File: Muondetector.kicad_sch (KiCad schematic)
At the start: 32 parts, among them U2 ${SIM.PARAMS}, U3 ${SIM.PARAMS}

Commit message: yes
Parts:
- removed U7: ~, symbol MuonDetector:3965_pressure_sensor
- added C7: C, symbol Device:C
- added Q1, Q2: 2N7002E, Package_TO_SOT_SMD:SOT-23, symbol Transistor_FET:2N7002E
- added R14, R15, R16, R17, R18, R19, R20: R, symbol Device:R
- added U4: ~, symbol MuonDetector:MPR_Pressure_sensor
- added U7: ~, symbol MuonDetector:MIC5225
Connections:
- net at L1.2, R11.1, U2.3 (V+)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: now also R19.2, R20.2
- new net: Q1.2 (S), R15.1, R19.1
- new net: Q2.2 (S), R16.1, R20.1
- new net: Q1.3 (D), R17.1
- new net: Q1.1 (G), Q2.1 (G), R14.2, R17.2, R18.2
- new net: Q2.3 (D), R18.1
- new net +3.3V: R15.2, R16.2
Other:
- note added: "+3.3V"

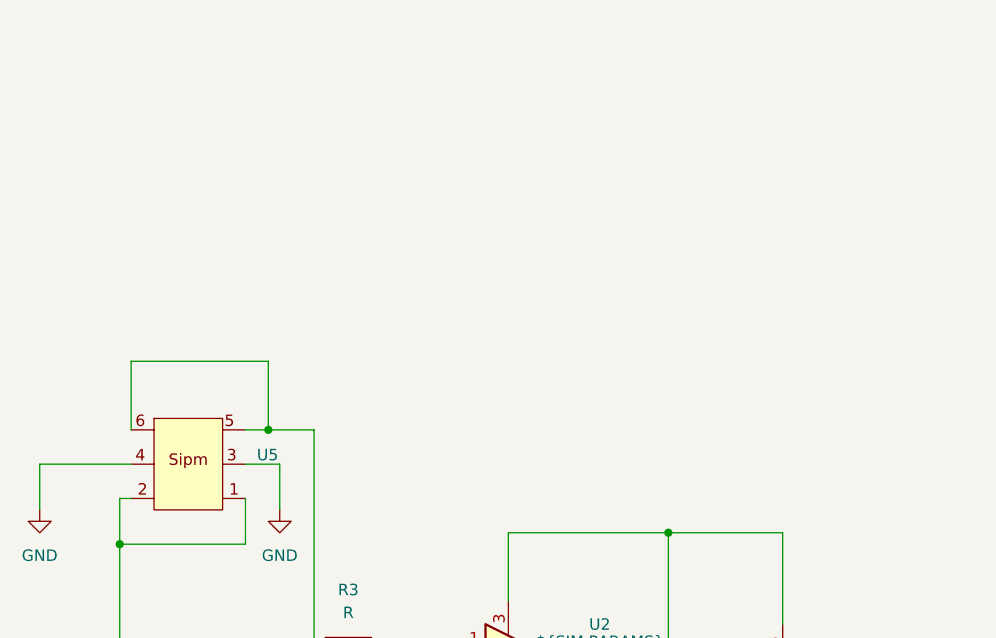
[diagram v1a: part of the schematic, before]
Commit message: Added the sipm
I added the silicon photomultiplier to the schematic
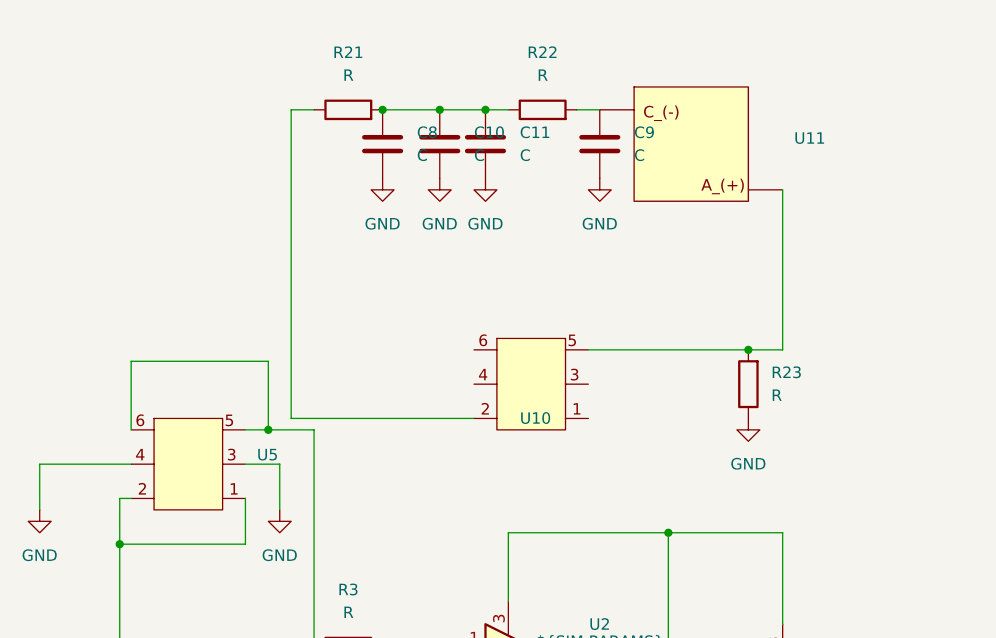
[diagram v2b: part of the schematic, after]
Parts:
- removed U5: ~, symbol MuonDetector:Sipm
- added C10, C11, C8, C9: C, symbol Device:C
- added R21, R22, R23: R, symbol Device:R
- added U10, U5: ~, symbol MuonDetector:Sipm Connector
- added U11: ~, symbol MuonDetector:SIPM1
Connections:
- net GND: now also C10.2, C11.2, C8.2, C9.2, R23.1
- new net: C9.1, R22.2
- new net: C10.1, C11.1, C8.1, R21.2, R22.1

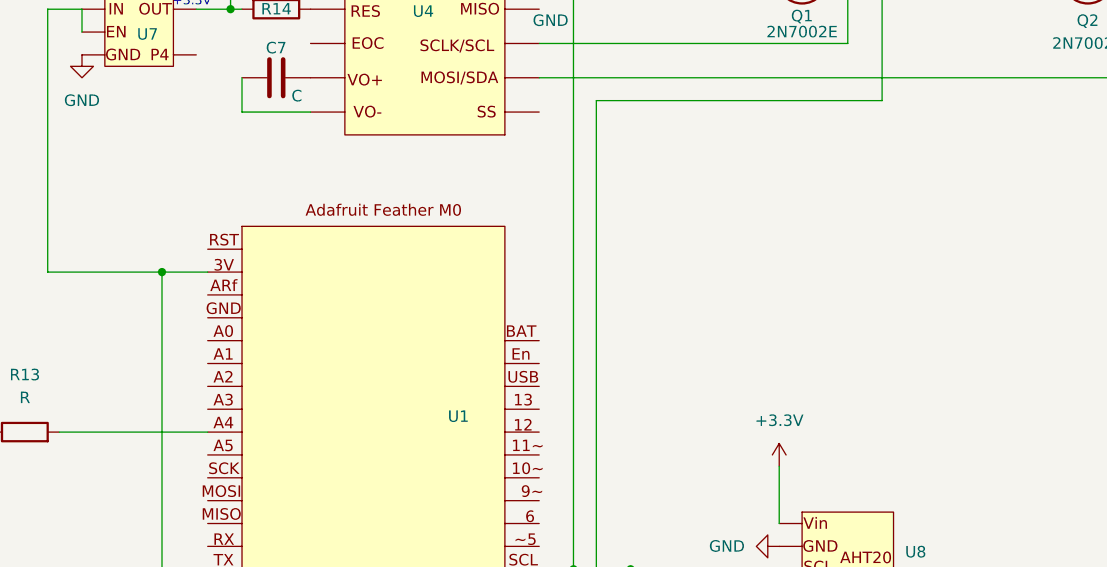
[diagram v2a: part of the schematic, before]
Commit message: Added Oled screen
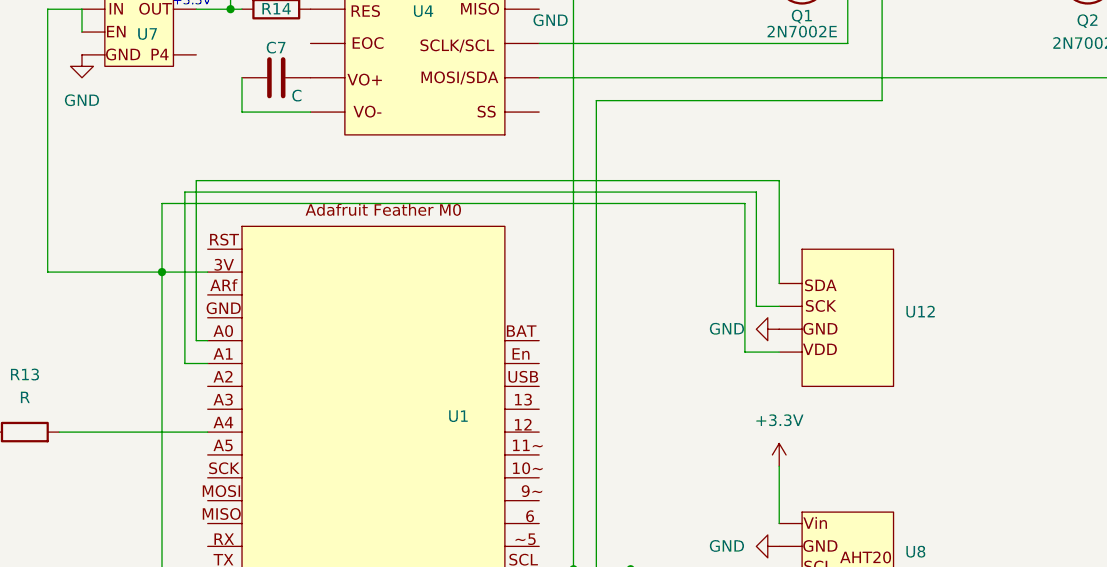
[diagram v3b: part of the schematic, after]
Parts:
- added U12: ~, symbol MuonDetector:OLED
